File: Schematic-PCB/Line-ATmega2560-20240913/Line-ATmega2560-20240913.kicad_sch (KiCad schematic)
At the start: 34 parts, among them J1 Conn01, J2 Conn02, J3 Conn03, J4 Conn04, J5 Conn05, J6 CH340E, J7 ICSP, SW1 SW_Push, SW2 SW_SPDT, SW3 SW_SPDT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

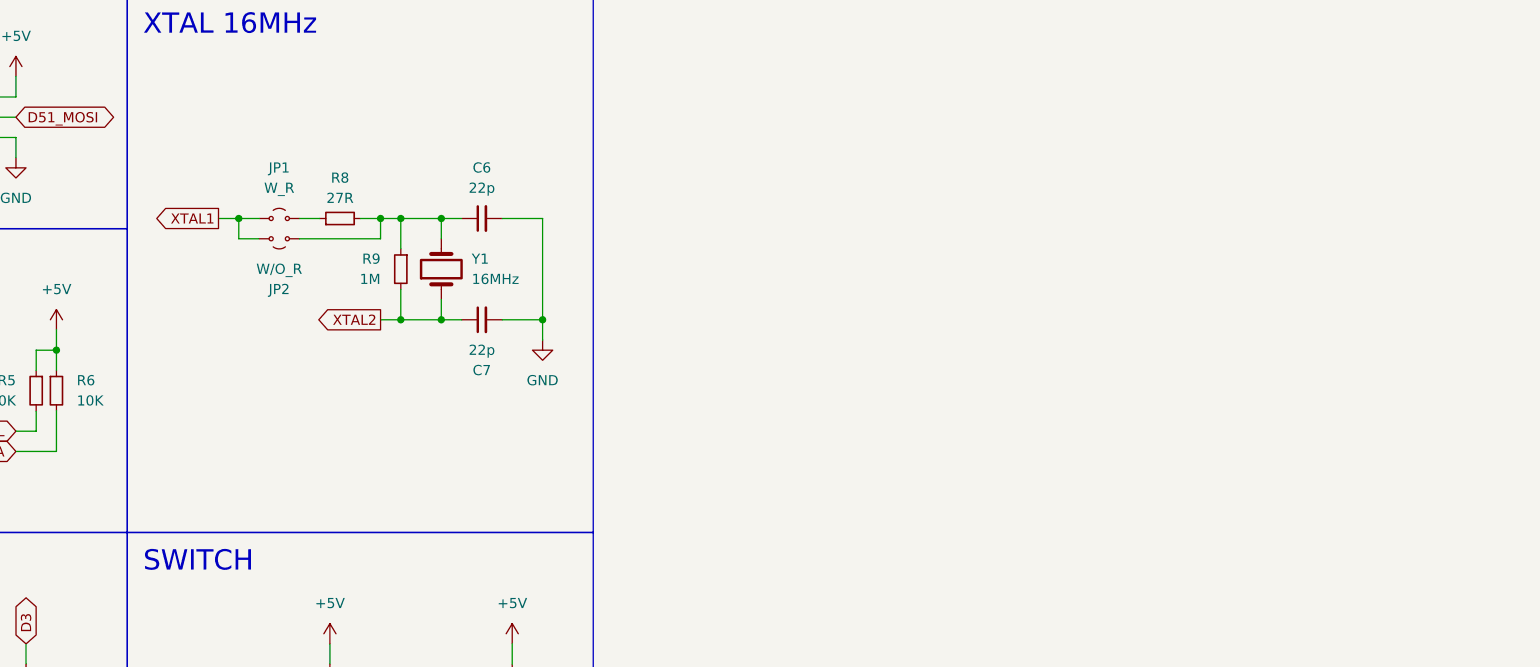
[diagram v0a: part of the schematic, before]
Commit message: ATmega2560の評価基板の回路図修正
セラロック発振器に変更した、回路図は山本さんに確認取中
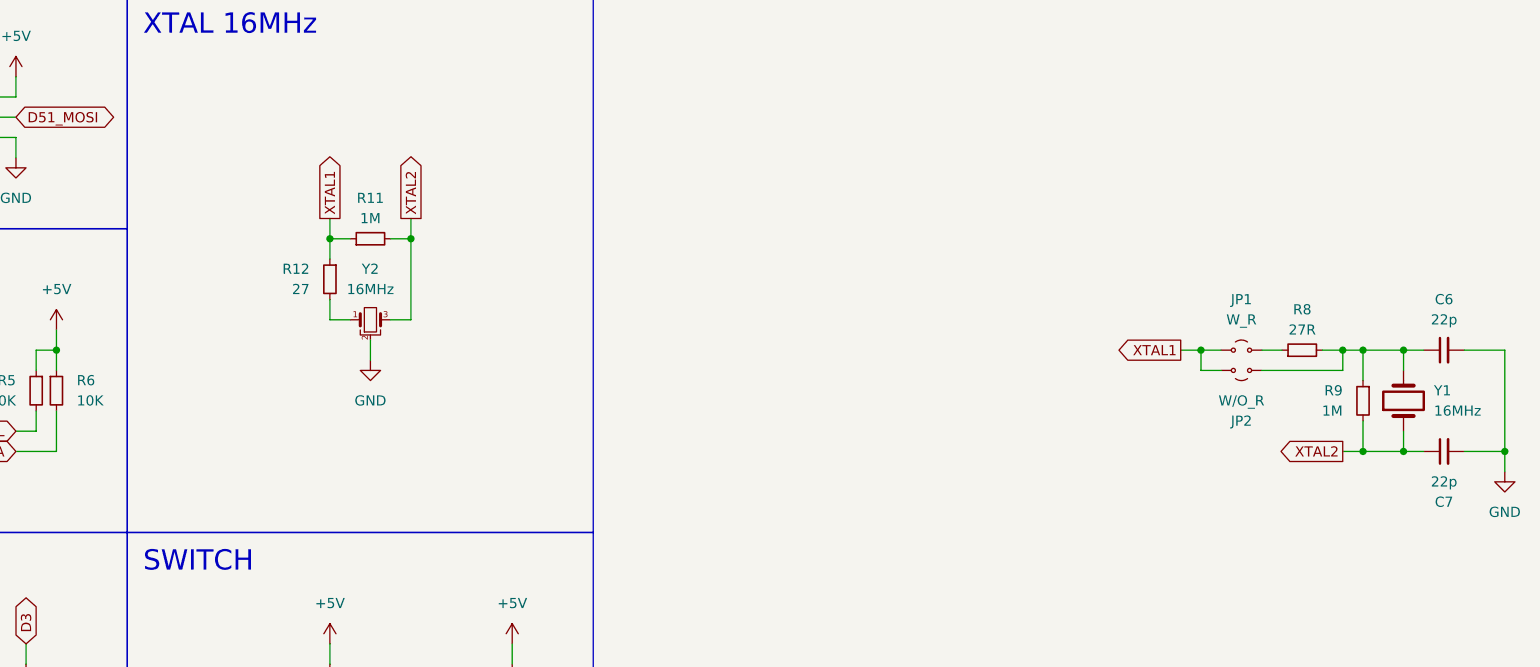
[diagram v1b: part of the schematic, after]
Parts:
- added R11: 1M, Resistor_SMD:R_0603_1608Metric, symbol Device:R_Small
- added R12: 27, symbol Device:R_Small
- added Y2: 16MHz, symbol Device:Crystal_GND2_Small
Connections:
- net GND: now also Y2.2
- net XTAL1: now also R11.1, R12.1
- net XTAL2: now also R11.2, Y2.3
- new net: R12.2, Y2.1
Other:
- moved on the sheet: C6, C7, JP1, JP2, R8, R9, Y1

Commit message: 評価基板のPCB仮完成
各ピンを出す用のコネクタ以外は配置・配線完了
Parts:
- removed C7: 22p, Capacitor_SMD:C_0603_1608Metric, symbol Device:C_Small
- removed JP1: W_R, Jumper:SolderJumper-2_P1.3mm_Open_Pad1.0x1.5mm, symbol Jumper:Jumper_2_Small_Open
- removed JP2: W/O_R, Jumper:SolderJumper-2_P1.3mm_Open_Pad1.0x1.5mm, symbol Jumper:Jumper_2_Small_Open
- removed R10, R7: 10K, Resistor_SMD:R_0603_1608Metric, symbol Device:R_Small
- removed R9: 1M, Resistor_SMD:R_0603_1608Metric, symbol Device:R_Small
- removed SW2, SW3: SW_SPDT, symbol Switch:SW_SPDT
- removed Y1: 16MHz, @2024TOINIOT2-Line-ATmega2560:AL4BT, symbol Device:Crystal
- added D4: LED1, LED_SMD:LED_0603_1608Metric, symbol Device:LED_Small_Filled
- added J10: VIN, Connector_PinSocket_2.54mm:PinSocket_1x02_P2.54mm_Vertical, symbol Connector:Conn_01x02_Pin
- added J6: Conn06, symbol Connector:Conn_01x10_Pin
- added J7: Conn07, symbol Connector:Conn_01x10_Pin
- C6: value 22p -> 100n
- J8: renamed from J6; footprint Connector_PinSocket_2.54mm:PinSocket_1x06_P2.54mm_Horizontal -> Connector_PinSocket_2.54mm:PinSocket_1x06_P2.54mm_Vertical
- R7: renamed from R12; footprint (none) -> Resistor_SMD:R_0603_1608Metric
- R8: value 27R -> 330
- Y1: renamed from Y2; footprint (none) -> Crystal:Resonator_Murata_CSTLSxxxX-3Pin_W5.5mm_H3.0mm
- renumbered J7 to J9, R11 to R9
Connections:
- net +5V: now also C6.1, J10.1 (Pin_1), J7.9 (Pin_9)
- net ADC0: now also J6.1 (Pin_1)
- net ADC1: now also J6.2 (Pin_2)
- net ADC10: now also J7.1 (Pin_1)
- net ADC11: now also J7.2 (Pin_2)
- net ADC12: now also J7.3 (Pin_3)
- net ADC13: now also J7.4 (Pin_4)
- net ADC14: now also J7.5 (Pin_5)
- net ADC15: now also J7.6 (Pin_6)
- net ADC2: now also J6.3 (Pin_3)
- net ADC3: now also J6.4 (Pin_4)
- net ADC4: now also J6.5 (Pin_5)
- net ADC5: now also J6.6 (Pin_6)
- net ADC6: now also J6.7 (Pin_7)
- net ADC7: now also J6.8 (Pin_8)
- net ADC8: now also J6.9 (Pin_9)
- net ADC9: now also J6.10 (Pin_10)
- net D13: now also R8.1
- net GND: now also D4.1 (K), J10.2 (Pin_2), J7.10 (Pin_10)
- net SCL: now also J7.7 (Pin_7)
- net SDA: now also J7.8 (Pin_8)
- net at R8.2: now also D4.2 (A); no longer C6.1
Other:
- moved on the sheet: D1, D2, D3, R1, R3, R4
